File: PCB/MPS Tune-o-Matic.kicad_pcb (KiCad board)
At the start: 2 copper layers, 87 parts, among them J1 ISP, J2 DB9_Male, J3 UI1, J4 UI2, J5 USB_B_Mini, Q1 PZT2222A,115, Q2 PZT2222A,115, Q3 PZT2222A,115, Q4 PZT2222A,115, Q5 PZT2222A,115, U1 ATmega328P, U2 MC34063AD, U3 FT232RL, U4 LM2940, Y1 FA-238 16.0000MB-C3

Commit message: WIP.
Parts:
- C14: footprint Capacitor_SMD:CP_Elec_4x5.8 -> Capacitor_SMD:C_0603_1608Metric
- J5: value USB_B_Mini -> USB_B_Micro; footprint Connector_USB:USB_Mini-B_Wuerth_65100516121_Horizontal -> Connector_USB:USB_Micro-B_Amphenol_10103594-0001LF_Horizontal
- moved C10 170.1 mm to (57.2, 26.5), turned to 90 degrees
- moved C12 165.0 mm to (51.2, 40.0), turned to 90 degrees
- moved C7 163.2 mm to (64.0, 20.5), turned to 270 degrees
- moved R9 160.9 mm to (49.5, 27.2)
- moved C16 159.5 mm to (66.9, 20.5), turned to 90 degrees
- moved C14 158.2 mm to (67.0, 24.0), turned to 270 degrees
- moved C13 156.9 mm to (69.5, 40.0)
- moved R7 156.6 mm to (71.0, 33.3), turned to 270 degrees
- moved R3 156.5 mm to (53.0, 40.0), turned to 90 degrees
- moved R4 156.0 mm to (49.5, 40.0), turned to 90 degrees
- moved D2 154.2 mm to (53.0, 27.2)
- moved C9 151.8 mm to (71.0, 28.8), turned to 270 degrees
- moved U3 150.1 mm to (54.3, 33.4), turned to 90 degrees
- moved U4 148.9 mm to (72.3, 44.8)
- moved J5 147.8 mm to (58.1, 21.0), turned to 180 degrees
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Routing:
- added copper zone on B.Cu, net GND
- added copper zone on F.Cu, net GND
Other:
- board outline added: 81.5 x 62.2 mm
- board text added: "(C) andy@britishideas.com 2022"
- board text added: "D-Jetronic MPS Tune-o-Matic V1.0"

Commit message: Working on PCB layout.
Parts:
- C1: footprint Capacitor_SMD:CP_Elec_4x5.8 -> Capacitor_SMD:C_0603_1608Metric
- TP1, TP2, TP8, TP9: footprint TestPoint:TestPoint_Pad_3.0x3.0mm -> TestPoint:TestPoint_Pad_2.0x2.0mm
- moved R32 216.6 mm to (52.8, 70.0), turned to 90 degrees
- moved R31 215.3 mm to (52.8, 66.8), turned to 90 degrees
- moved R30 210.8 mm to (52.8, 63.5), turned to 90 degrees
- moved TP4 205.6 mm to (55.8, 71.2)
- moved R29 202.2 mm to (65.0, 66.8)
- moved TP6 198.6 mm to (57.8, 55.2)
- moved R11 194.1 mm to (67.2, 52.8)
- moved R28 190.7 mm to (65.0, 68.5), turned to 180 degrees
- moved C17 189.9 mm to (70.2, 60.3), turned to 270 degrees
- moved R13 189.8 mm to (70.2, 57.0), turned to 270 degrees
- moved R15 187.0 mm to (70.2, 53.5), turned to 90 degrees
- moved R19 184.6 mm to (67.5, 62.2)
- moved R24 181.3 mm to (87.0, 58.2), turned to 270 degrees
- moved D8 180.7 mm to (87.0, 61.3), turned to 90 degrees
- moved D7 180.6 mm to (79.2, 67.0), turned to 180 degrees
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
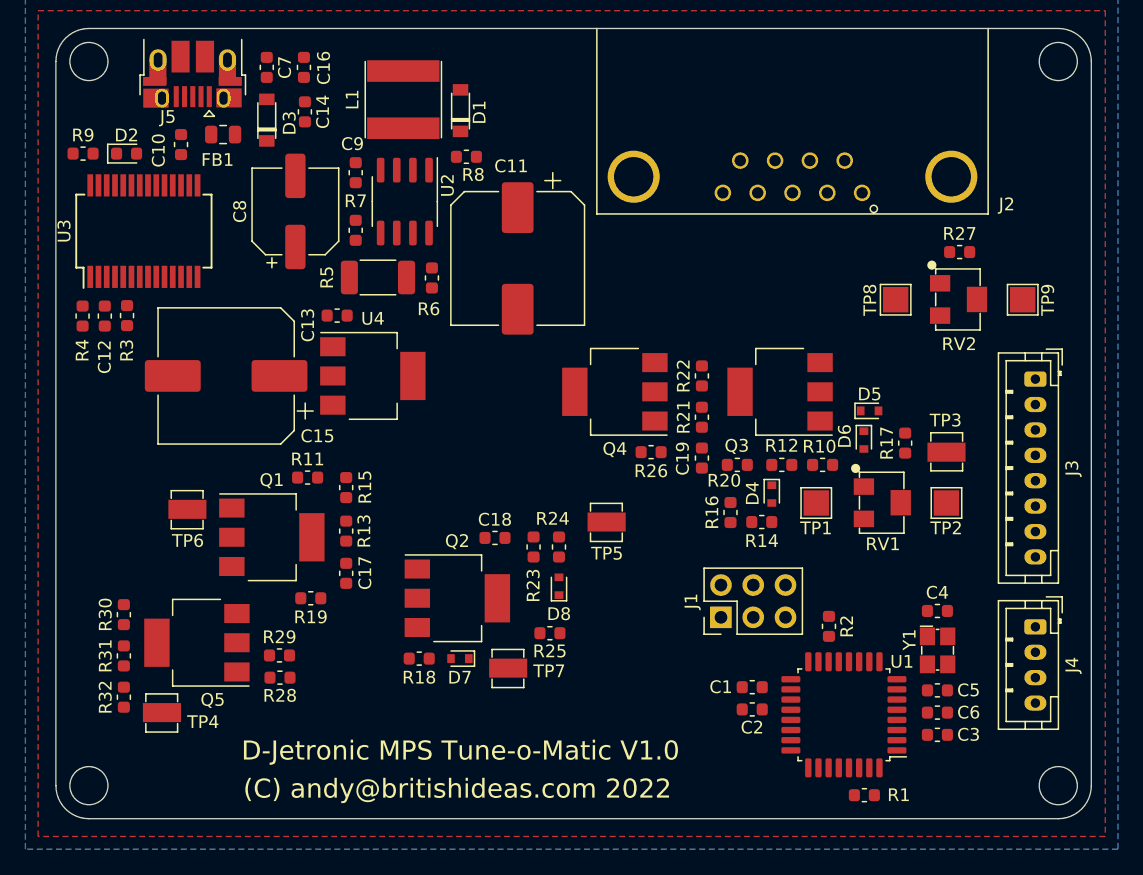
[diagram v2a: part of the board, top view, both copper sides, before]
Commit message: Completed PCB layout.
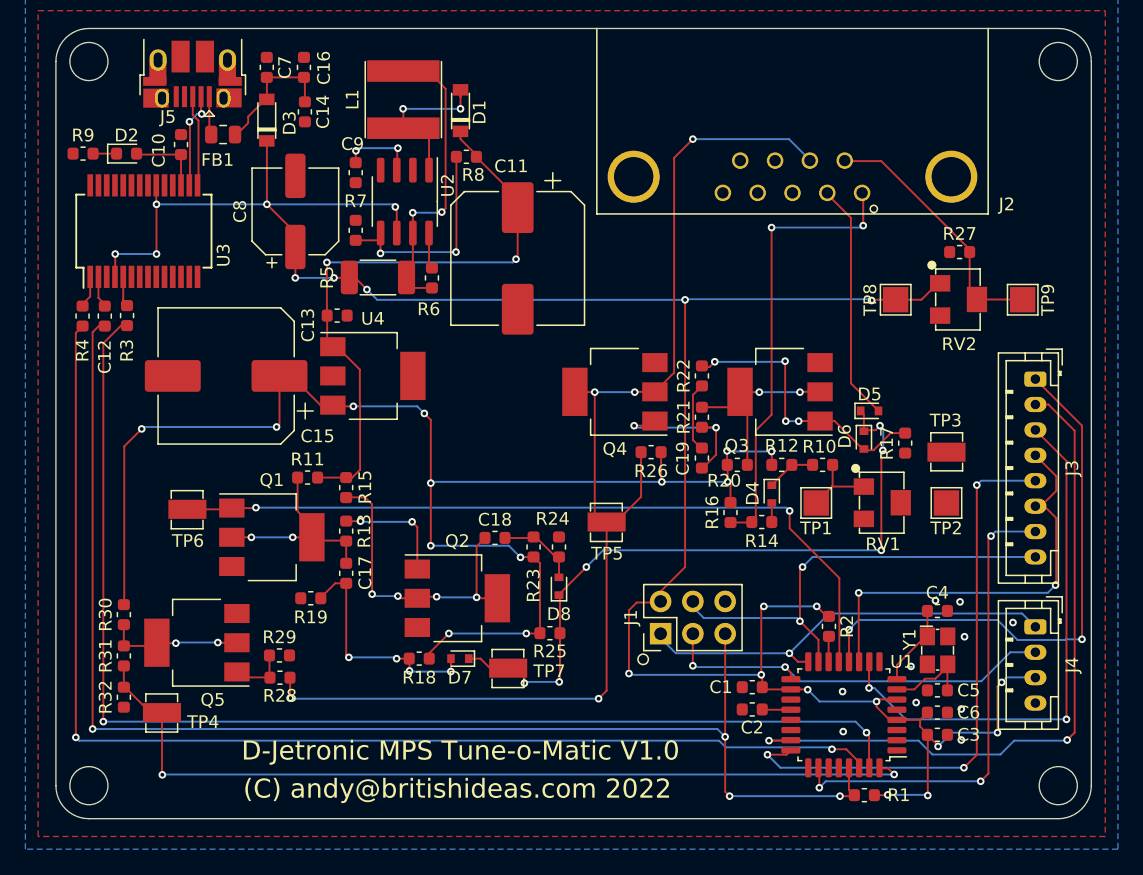
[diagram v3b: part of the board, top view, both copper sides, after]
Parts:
- moved J1 4.92 mm to (95.0, 65.0)
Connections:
- J2 pad 4: /IO1 -> GND
- J2 pad 5: +5V -> GND
- J2 pad 8: /IO2 -> GND
- J2 pad 9: /IO0 -> GND
- U1 pad 1: /IO0 -> (no net)
- U1 pad 2: /IO1 -> (no net)
- U1 pad 9: /IO2 -> (no net)
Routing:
- net +5V: track 0.00 -> 188.3 mm, vias 0 -> 21
- net +10V: track 0.00 -> 110.1 mm, vias 0 -> 13
- net /~RESET: track 0.00 -> 107.5 mm, vias 0 -> 4
- net Net-(R3-Pad1): track 0.00 -> 95.3 mm, vias 0 -> 2
- net Net-(R4-Pad1): track 0.00 -> 95.2 mm, vias 0 -> 2
- net /MPS-7: track 0.00 -> 93.7 mm, vias 0 -> 5
- net /MPS_PULSE: track 0.00 -> 69.1 mm, vias 0 -> 2
- net /MPS_STIMULUS: track 0.00 -> 61.2 mm, vias 0 -> 2
- net /X-: track 0.00 -> 54.7 mm, vias 0 -> 2
- net /MPS Stimulator/EDGES: track 0.00 -> 53.4 mm, vias 0 -> 6
- net +12V: track 0.00 -> 46.4 mm, vias 0 -> 2
- net /Y+: track 0.00 -> 45.2 mm, vias 0 -> 3
- net /~SD_CS: track 0.00 -> 43.7 mm, vias 0 -> 2
- net /Y-: track 0.00 -> 42.3 mm, vias 0 -> 2
- net /~LCD_CS: track 0.00 -> 37.6 mm, vias 0 -> 3
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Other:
- net class Default: clearance 0.2 -> 0.152; trace_width 0.25 -> 0.152; via_dia 0.8 -> 0.6; via_drill 0.4 -> 0.3
- rule trace_clearance: 0.2 -> 0.152
- rule trace_min: 0.2 -> 0.152
- board text added: "D-JETRONIC"

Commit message: Moved DB9 connector and regenerated CAD files.
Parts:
- moved J2 3.00 mm to (105.3, 14.4)
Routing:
- net /MPS-15: track 35.2 -> 38.5 mm
- net /MPS-10: track 20.6 -> 23.8 mm
- net /MPS-8: track 18.7 -> 21.8 mm
- net /MPS-7: track 93.7 -> 93.5 mm, vias 5 -> 4
- net GND: vias 10 -> 80

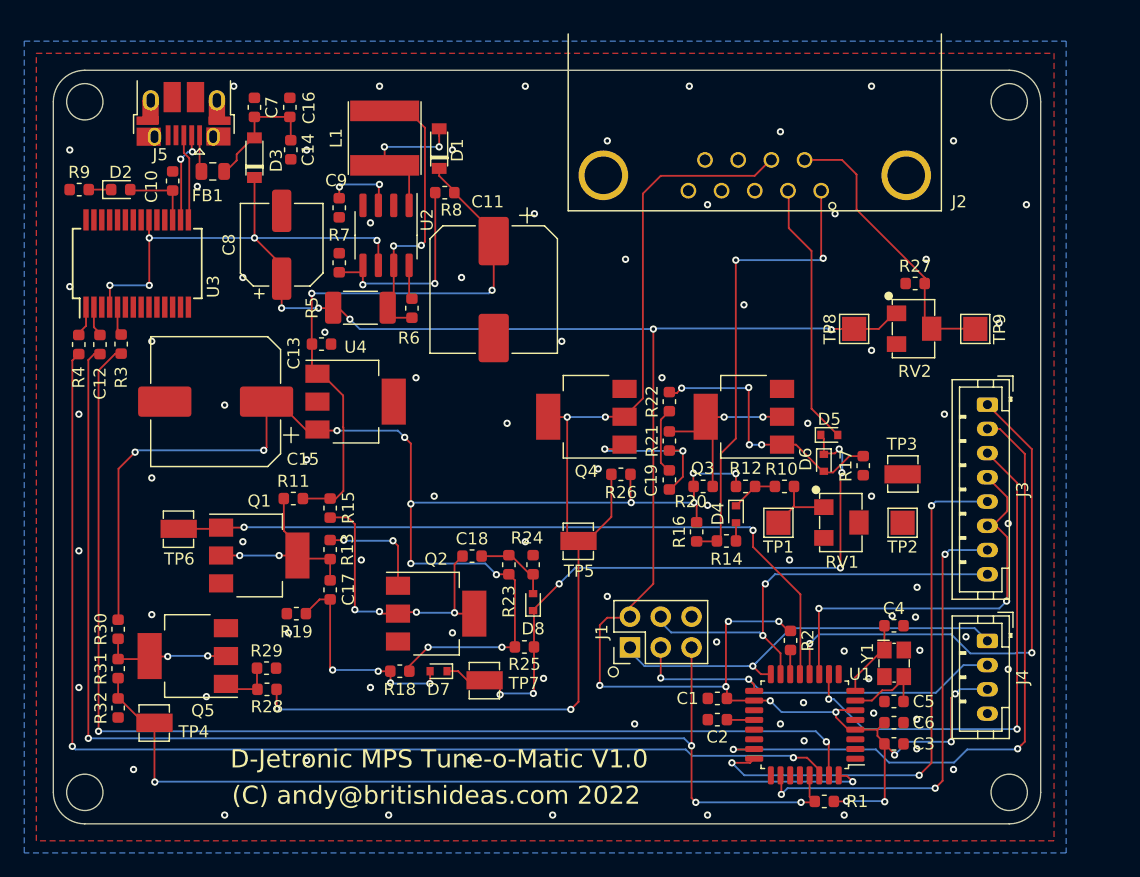
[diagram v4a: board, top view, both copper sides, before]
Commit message: Added status LED, remove LCD connectors, changed MPS connector to screw terminal block, added 12V power connections, removed 5V to 12V boost converter. Completely reworked PCB. Removed old PCB CAD files.
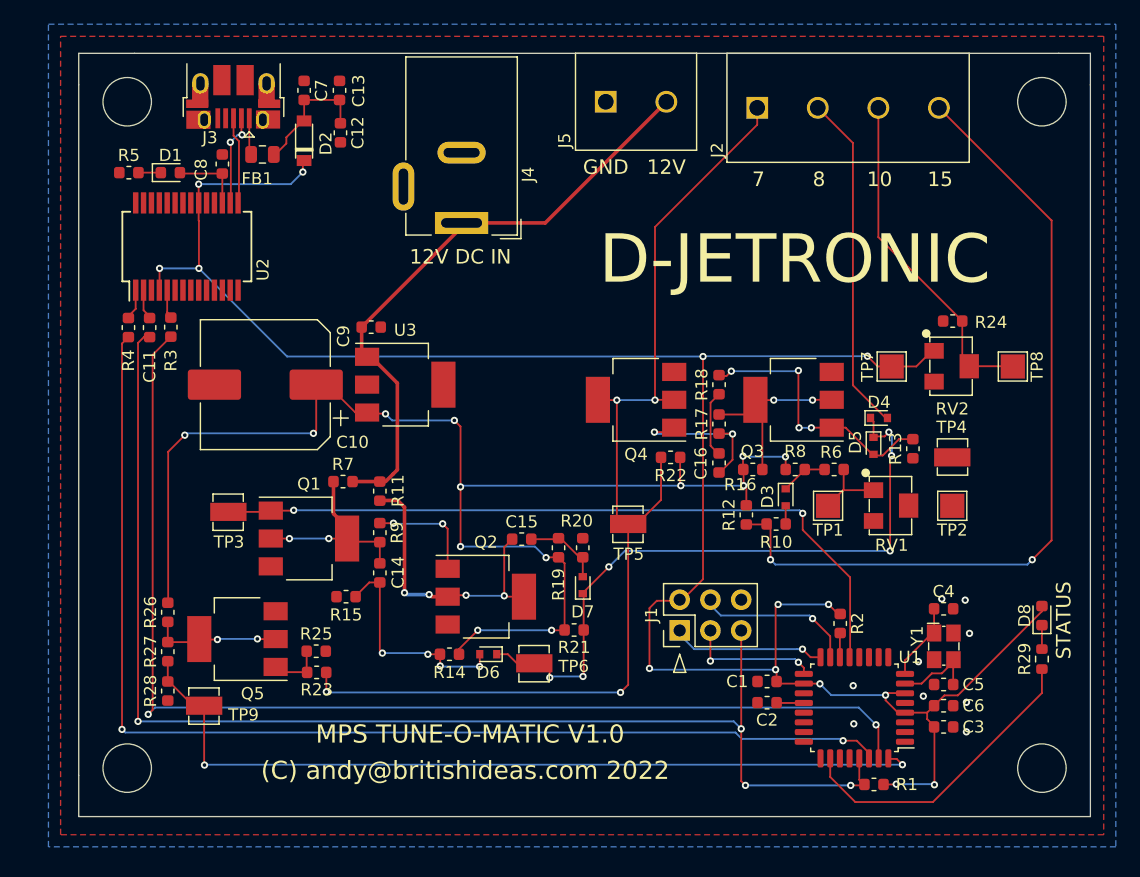
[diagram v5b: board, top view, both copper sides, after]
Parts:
- removed the C11 at (83.8, 35.5)
- removed the C8 at (66.2, 31.8)
- removed the C9 at (71.0, 28.8)
- removed the D1 at (79.2, 25.5)
- removed the J3 at (124.5, 45.0)
- removed L1: 30uH, Britishideas:Abracon ASPI-6045S Series Inductors
- removed the R5 at (72.8, 37.0)
- removed the R6 at (77.0, 37.0)
- removed the R7 at (71.0, 33.3)
- removed the R8 at (79.7, 27.5)
- removed the U2 at (74.9, 31.0)
- added D8: APT1608EC, LED_SMD:LED_0603_1608Metric, F.Cu at (129.0, 62.4)
- added J5: 12V IN, Britishideas:PhoenixContact_COMBICON_MKDSN_2, F.Cu at (93.0, 20.0)
- added R29: 150, Resistor_SMD:R_0603_1608Metric, F.Cu at (129.0, 66.0)
- J2: value DB9_Male -> MPS; footprint EmSA:DB9_RA_MALE_LD09P13A4 -> Britishideas:PhoenixContact_COMBICON_PT_4
- J4: value UI2 -> 12V 1A IN (5.5/2.5); footprint Connector_JST:JST_PH_B4B-PH-K_1x04_P2.00mm_Vertical -> Connector_BarrelJack:BarrelJack_Wuerth_6941xx301002
- R5: renamed from R9; value 620 -> 150
- moved J4 55.4 mm to (81.1, 30.0), turned to 180 degrees
- moved J2 6.10 mm to (105.5, 20.5), turned to 0 degrees
- moved R24 4.38 mm to (121.6, 38.1)
- moved RV2 4.38 mm to (121.5, 41.8)
- moved TP7 4.38 mm to (116.6, 41.9)
- moved TP8 4.38 mm to (126.6, 41.9)
- moved C3 4.33 mm to (120.9, 71.6)
- moved C5 4.33 mm to (120.9, 68.1)
- moved C6 4.33 mm to (120.9, 69.8)
- moved R1 4.33 mm to (115.1, 76.3)
- moved R23 4.33 mm to (69.1, 67.1)
- moved U1 4.33 mm to (113.5, 70.0)
- moved C10 4.33 mm to (64.9, 43.4)
- moved C13 4.33 mm to (71.0, 19.1)
- moved C4 4.33 mm to (120.9, 61.9)
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- renumbered C15 to C10, C12 to C11, C14 to C12, C16 to C13, C17 to C14, C18 to C15, C19 to C16, C10 to C8, C13 to C9, D2 to D1, D3 to D2, D4 to D3, D5 to D4, D6 to D5, D7 to D6, D8 to D7, J5 to J3, R14 to R10, R15 to R11, R16 to R12, R17 to R13, R18 to R14, R19 to R15, R20 to R16, R21 to R17, R22 to R18, R23 to R19, R24 to R20, R25 to R21, R26 to R22, R28 to R23, R27 to R24, R29 to R25, R30 to R26, R31 to R27, R32 to R28, R10 to R6, R11 to R7, R12 to R8, R13 to R9, TP6 to TP3, TP3 to TP4, TP7 to TP6, TP8 to TP7, TP9 to TP8, TP4 to TP9, U3 to U2, U4 to U3
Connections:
- J2 pad 1: /MPS-15 -> /MPS-7
- J2 pad 3: GND -> /MPS-10
- J2 pad 4: GND -> /MPS-15
- J4 pad 1: /MISO -> +12V
- J4 pad 2: /SCK -> GND
- J4 pad 3: +5V -> GND
- U1 pad 10: /Y- -> (no net)
- U1 pad 11: /LCD_DC_X+ -> (no net)
- U1 pad 12: /~SD_CS -> (no net)
- U1 pad 23: /X- -> (no net)
- U1 pad 24: /Y+ -> (no net)
- U1 pad 26: /~LCD_CS -> /STATUS
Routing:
- net /X-: track 54.7 -> 0.00 mm, vias 2 -> 0
- net /Y+: track 45.2 -> 0.00 mm, vias 3 -> 0
- net /~SD_CS: track 43.7 -> 0.00 mm, vias 2 -> 0
- net /Y-: track 42.3 -> 0.00 mm, vias 2 -> 0
- net /~LCD_CS: track 37.6 -> 0.00 mm, vias 3 -> 0
- net /LCD_DC_X+: track 33.5 -> 0.00 mm, vias 2 -> 0
- net /MPS-15: track 38.5 -> 68.5 mm
- net /STATUS: track 0.00 -> 25.6 mm
- net /MOSI: track 35.7 -> 12.7 mm, vias 2 -> 1
- net /MISO: track 33.4 -> 12.3 mm
- net /SCK: track 32.1 -> 11.2 mm
- net Net-(L1-Pad1): track 20.4 -> 0.00 mm, vias 2 -> 0
- net Net-(R7-Pad2): track 16.9 -> 0.00 mm, vias 2 -> 0
- net +5V: track 188.3 -> 176.3 mm, vias 21 -> 14
- net Net-(D1-Pad2): track 11.3 -> 0.00 mm, vias 2 -> 0
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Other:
- board size 81.5 x 62.2 mm -> 83.5 x 63 mm
- board text added: "10"
- board text added: "12V"
- board text added: "12V DC IN"
- board text added: "15"
- board text added: "7"
- board text added: "8"
- board text added: "GND"
- board text added: "MPS TUNE-O-MATIC V1.0"
- board text added: "STATUS"
- board text removed: "D-Jetronic MPS Tune-o-Matic V1.0"

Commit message: Added ground vias. Fixed voltage mistake for power LED.
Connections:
- D1 pad 2: +3V3 -> +5V
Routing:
- net +3V3: track 5.94 -> 2.52 mm
- net +5V: track 176.3 -> 178.3 mm
- net GND: vias 9 -> 120

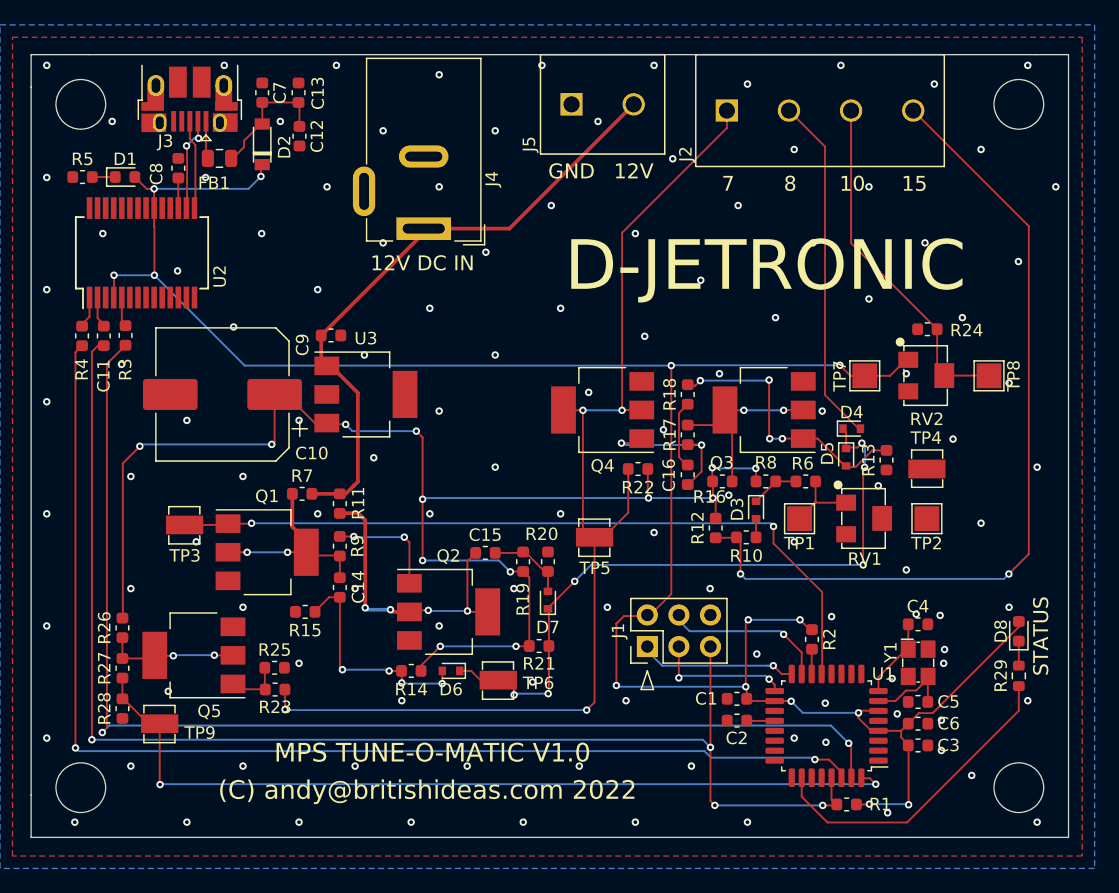
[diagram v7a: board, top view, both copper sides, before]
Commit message: Added pressure sensor.
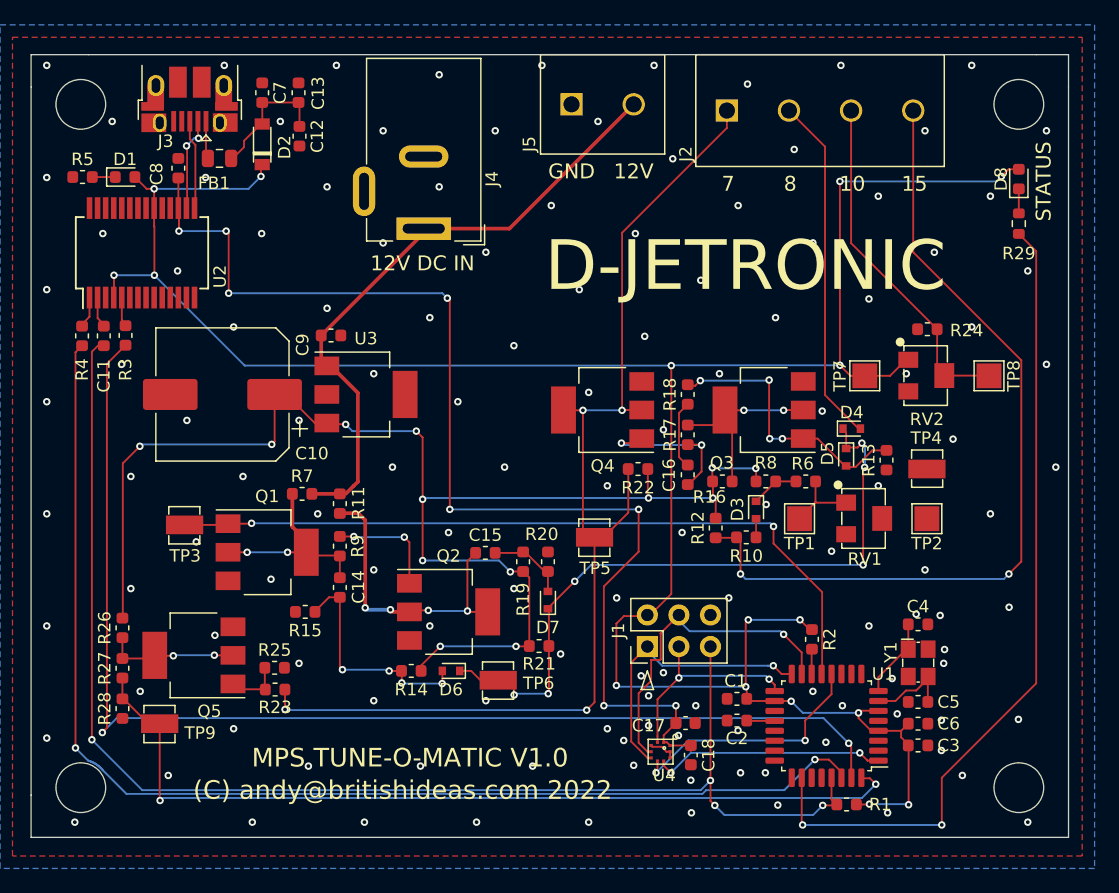
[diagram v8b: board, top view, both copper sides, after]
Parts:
- added C17: 100nF, Capacitor_SMD:C_0603_1608Metric, F.Cu at (102.2, 69.8)
- added C18: 100nF, Capacitor_SMD:C_0603_1608Metric, F.Cu at (102.6, 72.4)
- added U4: BMP390, Britishideas:LGA-2x2-10-pin, F.Cu at (100.2, 72.1)
- moved D8 36.4 mm to (129.0, 26.0)
- moved R29 36.4 mm to (129.0, 29.6)
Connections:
- U1 pad 1: (no net) -> /INT_PRESSURE
- U1 pad 12: (no net) -> /~CS_PRESSURE
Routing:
- net +3V3: track 2.52 -> 91.9 mm, vias 0 -> 8
- net /STATUS: track 25.6 -> 66.3 mm, vias 0 -> 2
- net /~CS_PRESSURE: track 0.00 -> 20.3 mm, vias 0 -> 2
- net /INT_PRESSURE: track 0.00 -> 18.8 mm, vias 0 -> 2
- net +5V: track 178.3 -> 195.4 mm, vias 14 -> 16
- net /MOSI: track 12.7 -> 26.1 mm
- net /MISO: track 12.3 -> 22.6 mm
- net /SCK: track 11.2 -> 17.1 mm
- net /~RESET: track 107.5 -> 109.9 mm
- net Net-(R4-Pad1): track 95.2 -> 97.5 mm
- net GND: track 0.00 -> 2.23 mm, vias 120 -> 132
- net /MPS_PULSE: track 69.1 -> 71.0 mm
